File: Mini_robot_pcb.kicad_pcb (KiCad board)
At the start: 2 copper layers, 39 parts, among them J1 USB_B_Mini, J10 Conn_01x06_Socket, J11 Conn_01x08_Socket, J12 Conn_01x06_Socket, J2 USB_B_Micro, J3 Conn_01x04_Pin, J4 Conn_01x08_Pin, J5 Conn_01x06_Pin, J6 Moteur 2, J7 Moteur 1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

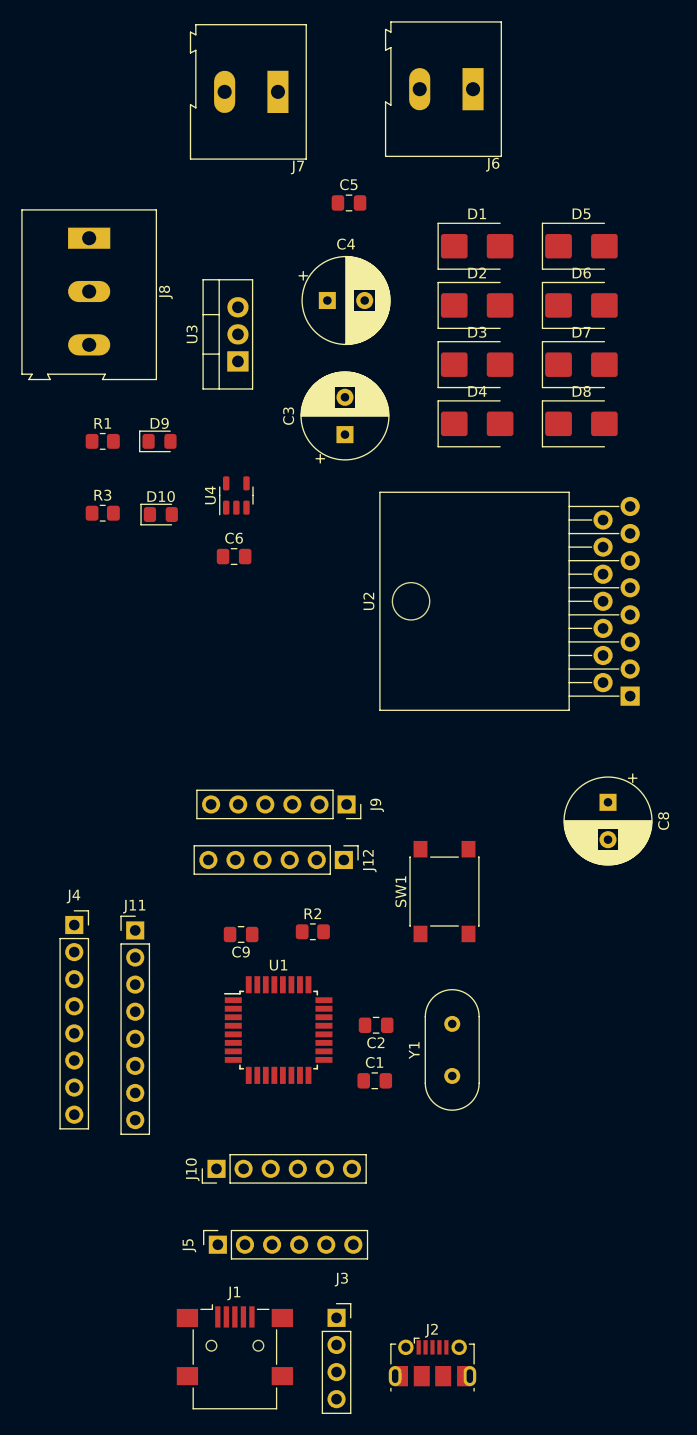
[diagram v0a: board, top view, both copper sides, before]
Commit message: Add bleutooth and FTDI
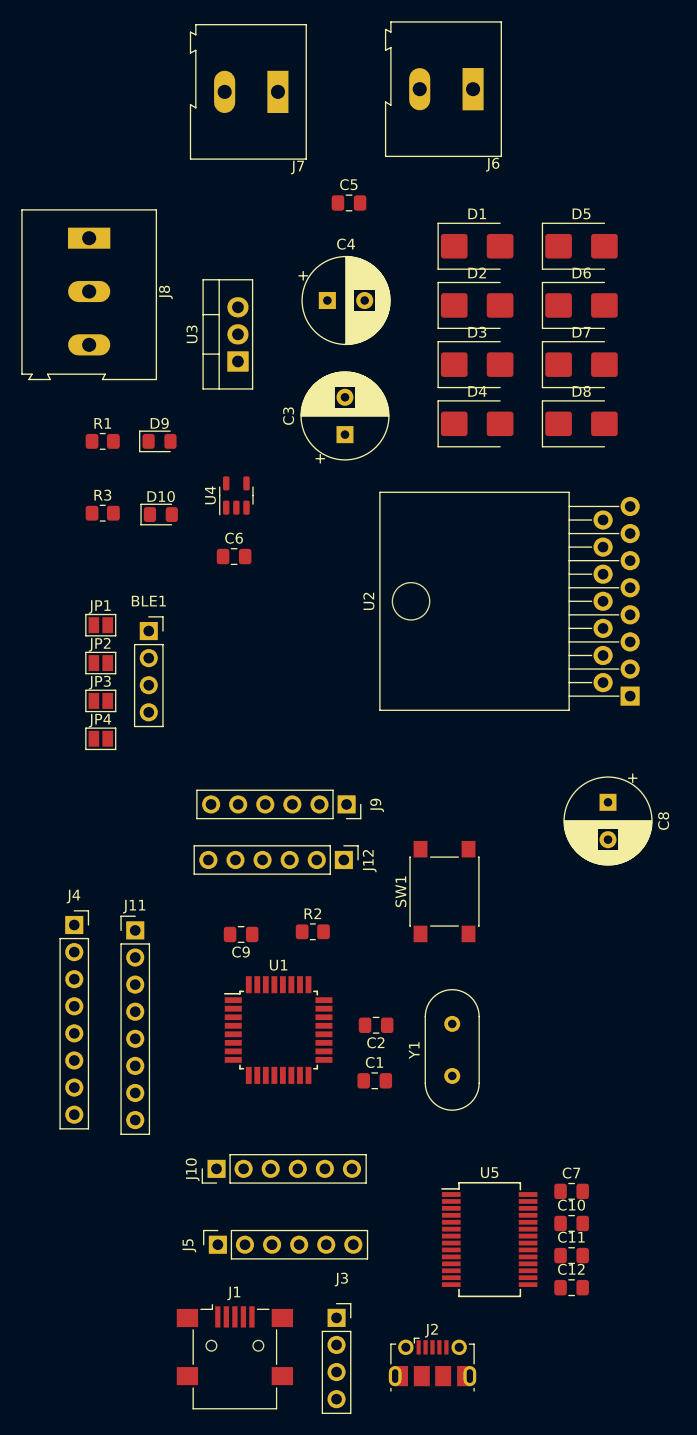
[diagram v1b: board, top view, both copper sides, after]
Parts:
- added BLE1: Conn_01x04_Pin, Connector_PinSocket_2.54mm:PinSocket_1x04_P2.54mm_Vertical, F.Cu at (110.5, 114.3)
- added C10: 0.1uF, Capacitor_SMD:C_0805_2012Metric_Pad1.18x1.45mm_HandSolder, F.Cu at (150.1, 169.8)
- added C11: 0.1uF, Capacitor_SMD:C_0805_2012Metric_Pad1.18x1.45mm_HandSolder, F.Cu at (150.1, 172.8)
- added C12: 100uF, Capacitor_SMD:C_0805_2012Metric_Pad1.18x1.45mm_HandSolder, F.Cu at (150.1, 175.9)
- added C7: 10uF, Capacitor_SMD:C_0805_2012Metric_Pad1.18x1.45mm_HandSolder, F.Cu at (150.1, 166.8)
- added JP1: Jumper_2_Open, Jumper:SolderJumper-2_P1.3mm_Open_Pad1.0x1.5mm, F.Cu at (106.0, 113.8)
- added JP2: Jumper_2_Open, Jumper:SolderJumper-2_P1.3mm_Open_Pad1.0x1.5mm, F.Cu at (106.0, 117.3)
- added JP3: Jumper_2_Open, Jumper:SolderJumper-2_P1.3mm_Open_Pad1.0x1.5mm, F.Cu at (106.0, 120.8)
- added JP4: Jumper_2_Open, Jumper:SolderJumper-2_P1.3mm_Open_Pad1.0x1.5mm, F.Cu at (106.0, 124.4)
- added U5: FT232RL, Package_SO:SSOP-28_5.3x10.2mm_P0.65mm, F.Cu at (142.4, 171.3)
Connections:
- net Net-(J11-Pin_1) renamed /RXD
- net Net-(J11-Pin_2) renamed /TXD
- J1 pad 1: Net-(J1-VBUS) -> GND
- J1 pad 2: Net-(J1-D-) -> GND
- J1 pad 3: Net-(J1-D+) -> GND
- J2 pad 1: Net-(J1-VBUS) -> GND
- J2 pad 2: Net-(J1-D-) -> GND
- J2 pad 3: Net-(J1-D+) -> GND
- J3 pad 1: Net-(J1-VBUS) -> GND
- J3 pad 2: Net-(J1-D+) -> GND
- J3 pad 3: Net-(J1-D-) -> GND
- R2 pad 2: Net-(R2-Pad2) -> /DTR
- SW1 pad 1: Net-(R2-Pad2) -> /DTR
- U1 pad 29: +5V -> /DTR
